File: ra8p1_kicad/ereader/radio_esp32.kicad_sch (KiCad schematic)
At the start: 28 parts, among them U3 ESP32-C6-WROOM-1-N8, U4 TPS22917DBVT, U5 TXU0304PWR, U6 TPS389001DSET, U7 SN74LVC1G97DBVR, U8 SN74LVC1G97DBVR

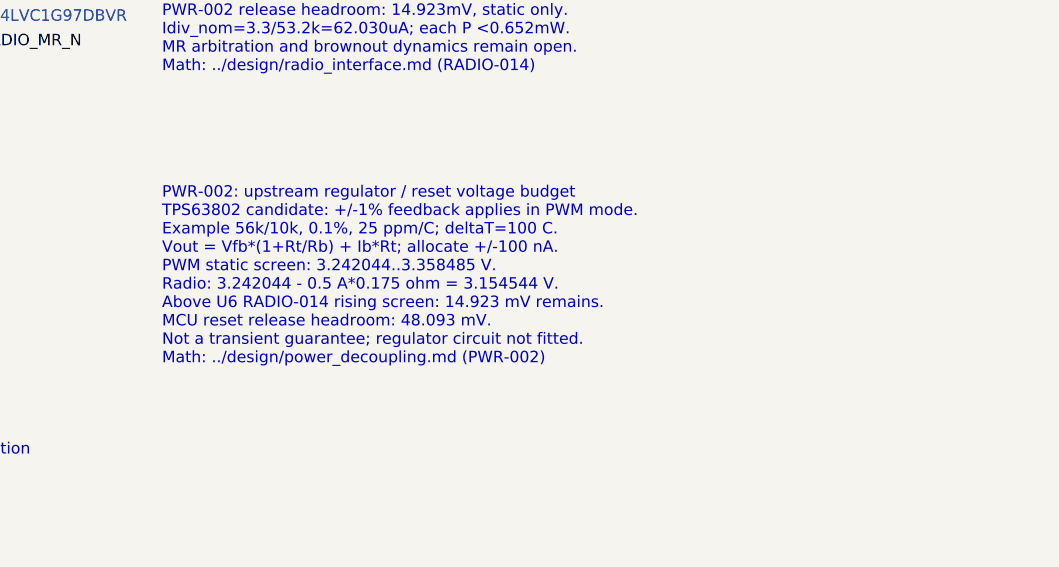
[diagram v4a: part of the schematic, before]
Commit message: Implement main digital supply with linked engineering calculations
Wire the TPS63802 converter and its hierarchical enable, source its exact BOM, and refresh the full nine-page schematic PDF. Preserve the SDRAM pin and timing contract for the memory implementation. Track #825 and #827; system qualification remains open.
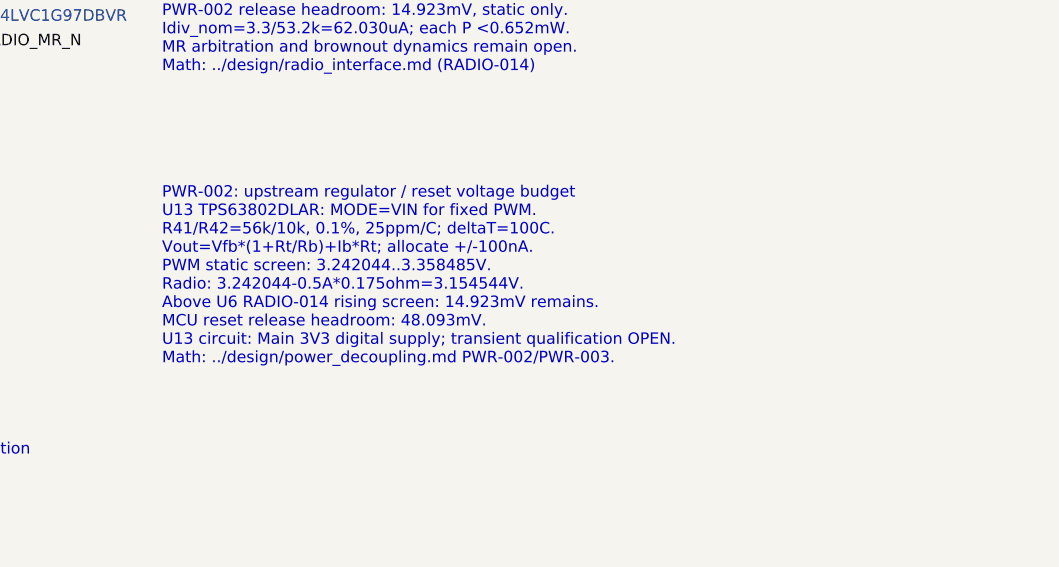
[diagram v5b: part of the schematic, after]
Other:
- note added: "PWR-002: upstream regulator / reset voltage budget U13 TPS63802DLAR: MODE=VIN for fixed PWM. R41/R42=56k/10k, 0.1%, 25ppm/C; deltaT=100C. Vout=Vfb*(1+Rt/Rb)+Ib*Rt; allocate +/-100nA. PWM static screen: 3.242044..3.358485V. Radio: 3.242044-0.5A*0.175ohm=3.154544V. Above U6 RADIO-014 rising screen: 14.923mV remains. MCU reset release headroom: 48.093mV. U13 circuit: Main 3V3 digital supply; transie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"
- note removed: "PWR-002: upstream regulator / reset voltage budget TPS63802 candidate: +/-1% feedback applies in PWM mode. Example 56k/10k, 0.1%, 25 ppm/C; deltaT=100 C. Vout = Vfb*(1+Rt/Rb) + Ib*Rt; allocate +/-100 nA. PWM static screen: 3.242044..3.358485 V. Radio: 3.242044 - 0.5 A*0.175 ohm = 3.154544 V. Above U6 RADIO-014 rising screen: 14.923 mV remains. MCU reset release headroom: 48.093 mV. Not a transien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"
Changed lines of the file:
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@@
 		(comment 1 "Incomplete electrical design - not for manufacture")
 	)
-	(text "PWR-002: upstream regulator / reset voltage budget\nTPS63802 candidate: +/-1% feedback applies in PWM mode.\nExample 56k/10k, 0.1%, 25 ppm/C; deltaT=100 C.\nVout = Vfb*(1+Rt/Rb) + Ib*Rt; allocate +/-100 nA.\nPWM static screen: 3.242044..3.358485 V.\nRadio: 3.242044 - 0.5 A*0.175 ohm = 3.154544 V.\nAbove U6 RADIO-014 rising screen: 14.923 mV remains.\nMCU reset release headroom: 48.093 mV.\nNot a transient guarantee; regulator circuit not fitted.\nMath: ../design/power_decoupling.md (PWR-002)"
+	(text "PWR-002: upstream regulator / reset voltage budget\nU13 TPS63802DLAR: MODE=VIN for fixed PWM.\nR41/R42=56k/10k, 0.1%, 25ppm/C; deltaT=100C.\nVout=Vfb*(1+Rt/Rb)+Ib*Rt; allocate +/-100nA.\nPWM static screen: 3.242044..3.358485V.\nRadio: 3.242044-0.5A*0.175ohm=3.154544V.\nAbove U6 RADIO-014 rising screen: 14.923mV remains.\nMCU reset release headroom: 48.093mV.\nU13 circuit: Main 3V3 digital supply; transient qualification OPEN.\nMath: ../design/power_decoupling.md PWR-002/PWR-003."
 		(exclude_from_sim no)
 		(at 266.7 142.24 0)

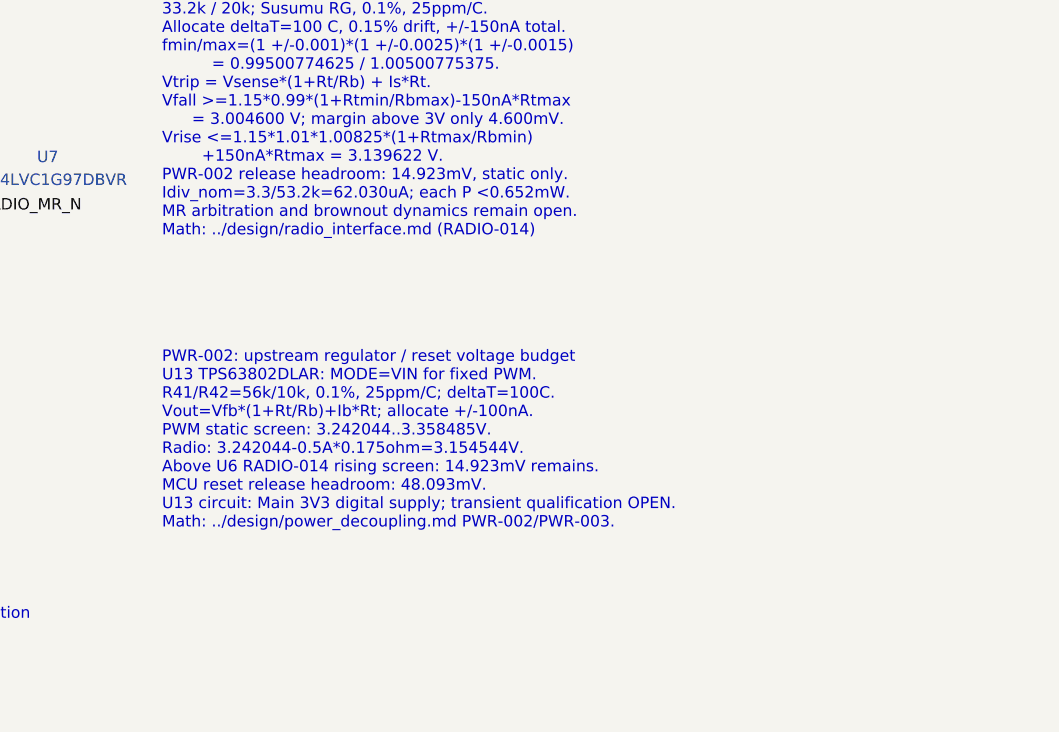
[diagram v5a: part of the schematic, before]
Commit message: Wire LTC3119 power-stage draft and held RUN control
Add native RUN buffer and held-domain clamp with verified connectivity, sourced BOM fields, and linked PWR-004 calculations. Export the full schematic PDF and native BOM.

Keep rail adoption blocked by SDRAM logic-high conflict #846. Whole-project ERC remains 133 errors and two warnings; this checkpoint adds no findings.
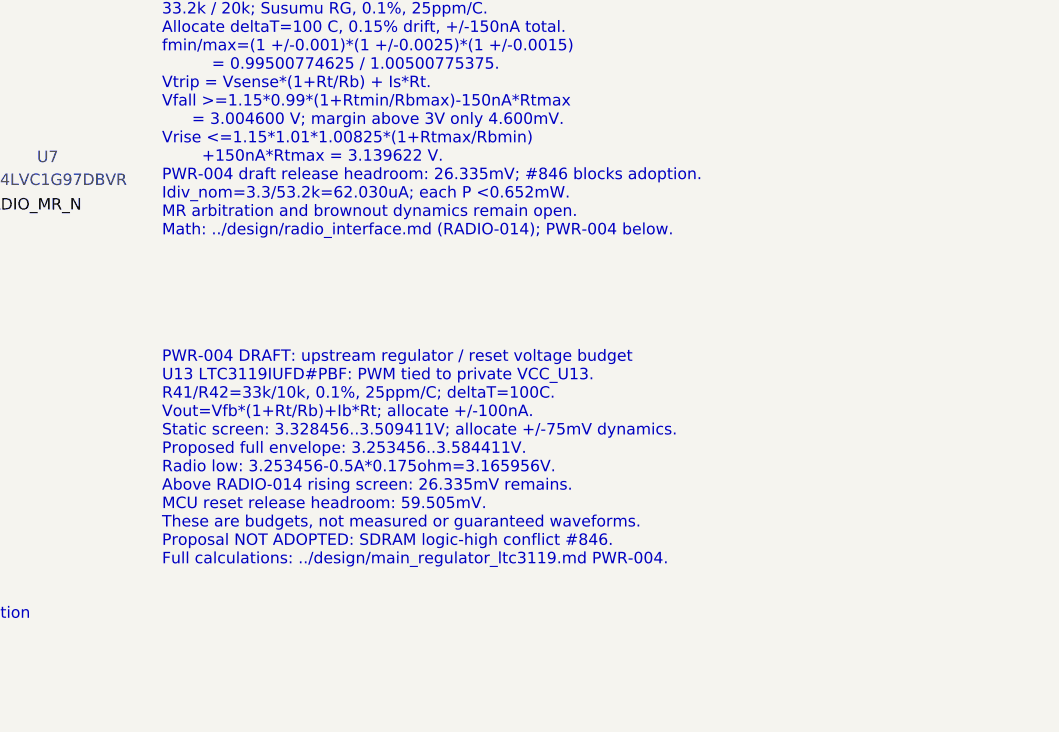
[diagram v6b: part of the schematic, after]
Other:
- note added: "PWR-004 DRAFT: upstream regulator / reset voltage budget U13 LTC3119IUFD#PBF: PWM tied to private VCC_U13. R41/R42=33k/10k, 0.1%, 25ppm/C; deltaT=100C. Vout=Vfb*(1+Rt/Rb)+Ib*Rt; allocate +/-100nA. Static screen: 3.328456..3.509411V; allocate +/-75mV dynamics. Proposed full envelope: 3.253456..3.584411V. Radio low: 3.253456-0.5A*0.175ohm=3.165956V. Above RADIO-014 rising screen: 26.335mV remains. 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"
- note removed: "PWR-002: upstream regulator / reset voltage budget U13 TPS63802DLAR: MODE=VIN for fixed PWM. R41/R42=56k/10k, 0.1%, 25ppm/C; deltaT=100C. Vout=Vfb*(1+Rt/Rb)+Ib*Rt; allocate +/-100nA. PWM static screen: 3.242044..3.358485V. Radio: 3.242044-0.5A*0.175ohm=3.154544V. Above U6 RADIO-014 rising screen: 14.923mV remains. MCU reset release headroom: 48.093mV. U13 circuit: Main 3V3 digital supply; transie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"
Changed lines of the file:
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@@
 		(comment 1 "Incomplete electrical design - not for manufacture")
 	)
-	(text "PWR-002: upstream regulator / reset voltage budget\nU13 TPS63802DLAR: MODE=VIN for fixed PWM.\nR41/R42=56k/10k, 0.1%, 25ppm/C; deltaT=100C.\nVout=Vfb*(1+Rt/Rb)+Ib*Rt; allocate +/-100nA.\nPWM static screen: 3.242044..3.358485V.\nRadio: 3.242044-0.5A*0.175ohm=3.154544V.\nAbove U6 RADIO-014 rising screen: 14.923mV remains.\nMCU reset release headroom: 48.093mV.\nU13 circuit: Main 3V3 digital supply; transient qualification OPEN.\nMath: ../design/power_decoupling.md PWR-002/PWR-003."
+	(text "PWR-004 DRAFT: upstream regulator / reset voltage budget\nU13 LTC3119IUFD#PBF: PWM tied to private VCC_U13.\nR41/R42=33k/10k, 0.1%, 25ppm/C; deltaT=100C.\nVout=Vfb*(1+Rt/Rb)+Ib*Rt; allocate +/-100nA.\nStatic screen: 3.328456..3.509411V; allocate +/-75mV dynamics.\nProposed full envelope: 3.253456..3.584411V.\nRadio low: 3.253456-0.5A*0.175ohm=3.165956V.\nAbove RADIO-014 rising screen: 26.335mV remains.\nMCU reset release headroom: 59.505mV.\nThese are budgets, not measured or guaranteed waveforms.\nProposal NOT ADOPTED: SDRAM logic-high conflict #846.\nFull calculations: ../design/main_regulator_ltc3119.md PWR-004."
 		(exclude_from_sim no)
 		(at 266.7 142.24 0)
@@
 			)
 			(justify left top)
-			(href "https://github.com/bsikar/ra8-firmware/blob/design/ereader-circuit/ra8p1_kicad/design/power_decoupling.md#pwr-002-main-rail-regulation-and-reset-headroom")
+			(href "https://github.com/bsikar/ra8-firmware/blob/design/ereader-circuit/ra8p1_kicad/design/main_regulator_ltc3119.md")
 		)
 	)
@@
 		)
 	)
-	(text "RADIO-014: R12/R13 switched-radio sense divider\n33.2k / 20k; Susumu RG, 0.1%, 25ppm/C.\nAllocate deltaT=100 C, 0.15% drift, +/-150nA total.\nfmin/max=(1 +/-0.001)*(1 +/-0.0025)*(1 +/-0.0015)\n          = 0.99500774625 / 1.00500775375.\nVtrip = Vsense*(1+Rt/Rb) + Is*Rt.\nVfall >=1.15*0.99*(1+Rtmin/Rbmax)-150nA*Rtmax\n      = 3.004600 V; margin above 3V only 4.600mV.\nVrise <=1.15*1.01*1.00825*(1+Rtmax/Rbmin)\n        +150nA*Rtmax = 3.139622 V.\nPWR-002 release headroom: 14.923mV, static only.\nIdiv_nom=3.3/53.2k=62.030uA; each P <0.652mW.\nMR arbitration and brownout dynamics remain open.\nMath: ../design/radio_interface.md (RADIO-014)"
+	(text "RADIO-014: R12/R13 switched-radio sense divider\n33.2k / 20k; Susumu RG, 0.1%, 25ppm/C.\nAllocate deltaT=100 C, 0.15% drift, +/-150nA total.\nfmin/max=(1 +/-0.001)*(1 +/-0.0025)*(1 +/-0.0015)\n          = 0.99500774625 / 1.00500775375.\nVtrip = Vsense*(1+Rt/Rb) + Is*Rt.\nVfall >=1.15*0.99*(1+Rtmin/Rbmax)-150nA*Rtmax\n      = 3.004600 V; margin above 3V only 4.600mV.\nVrise <=1.15*1.01*1.00825*(1+Rtmax/Rbmin)\n        +150nA*Rtmax = 3.139622 V.\nPWR-004 draft release headroom: 26.335mV; #846 blocks adoption.\nIdiv_nom=3.3/53.2k=62.030uA; each P <0.652mW.\nMR arbitration and brownout dynamics remain open.\nMath: ../design/radio_interface.md (RADIO-014); PWR-004 below."
 		(exclude_from_sim no)
 		(at 266.7 101.6 0)
